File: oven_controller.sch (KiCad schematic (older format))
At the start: 31 parts, among them CON1 BUQ2-USB-MICRO-B, IC1 BUQ2-ATXMEGA128A4U-A, P1 CONN_THERMO, P2 CONN_POWER, U1 FLASH_MEMORY, U2 MAX6675ISA+, U3 TAG-CONNECT-ATMEL-PDI-CONNECT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, U4 LD1117-SOT-223, U5 LS013B4DN04, U6 SW_PUSH_4_PIN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

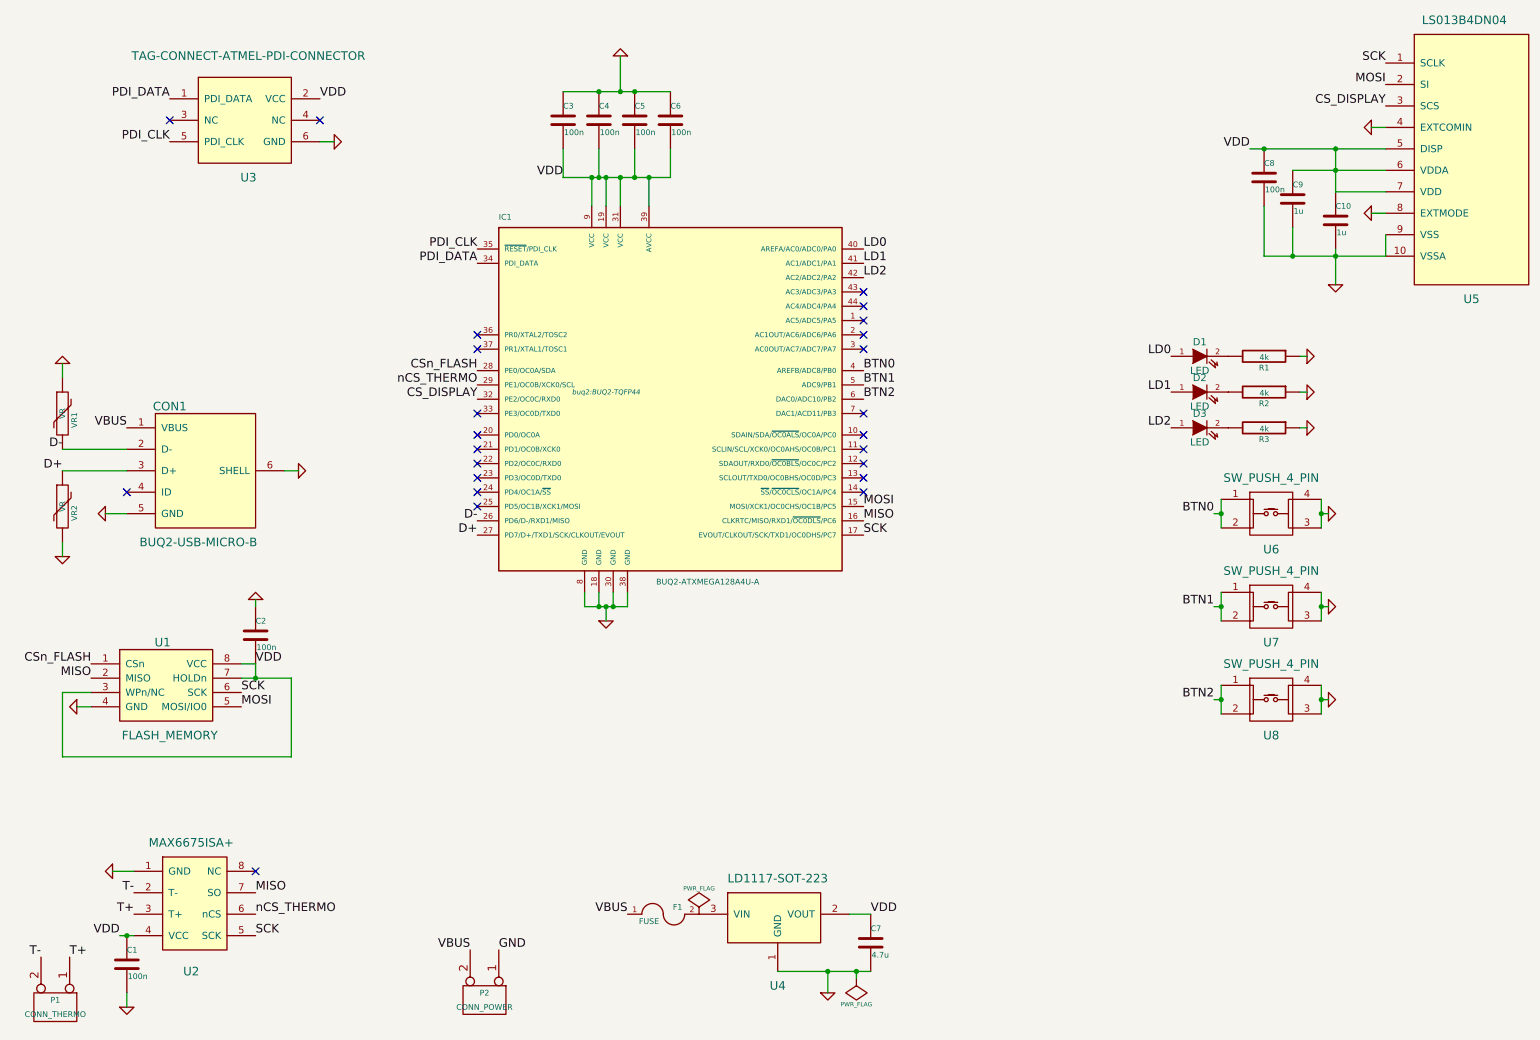
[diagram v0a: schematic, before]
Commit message: Layout done, but not checked
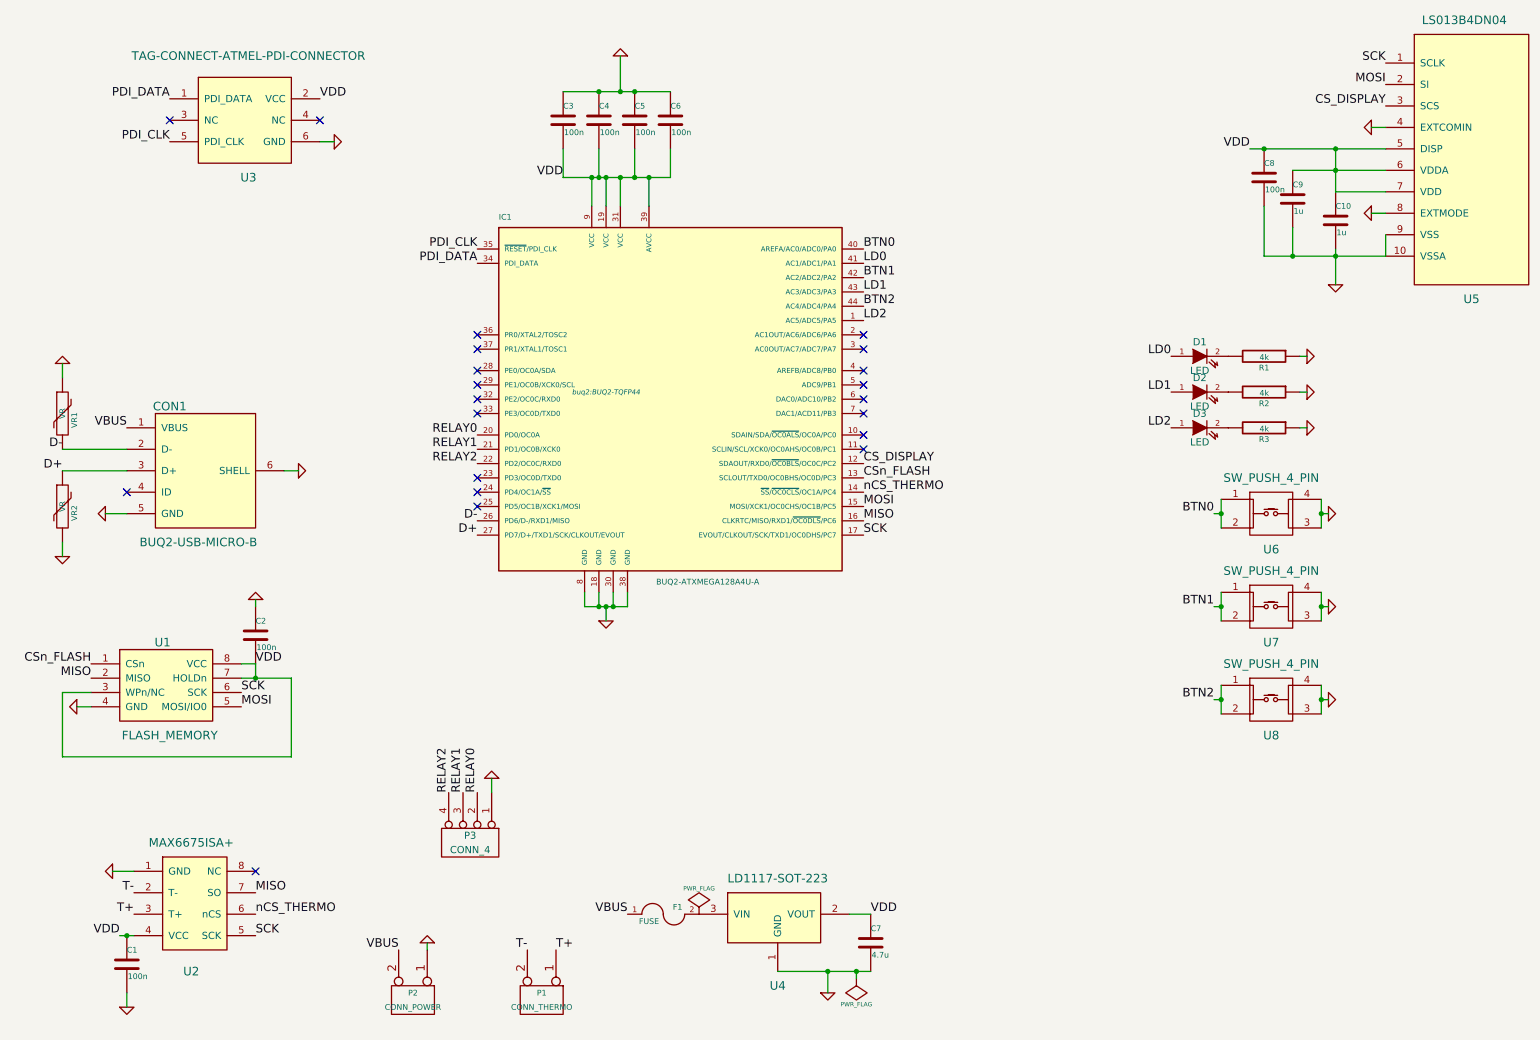
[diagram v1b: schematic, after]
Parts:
- added P3: CONN_4, buq2:PIN_HEADER_4, symbol CONN_4
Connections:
- net BTN0: now also IC1.40 (AREFA/AC0/ADC0/PA0); no longer IC1.4 (AREFB/ADC8/PB0)
- net BTN1: now also IC1.42 (AC2/ADC2/PA2); no longer IC1.5 (ADC9/PB1)
- net BTN2: now also IC1.44 (AC4/ADC4/PA4); no longer IC1.6 (DAC0/ADC10/PB2)
- net CS_DISPLAY: now also IC1.12 (SDAOUT/RXD0/~OC0BLS~/OC0C/PC2); no longer IC1.32 (PE2/OC0C/RXD0)
- net CSn_FLASH: now also IC1.13 (SCLOUT/TXD0/OC0BHS/OC0D/PC3); no longer IC1.28 (PE0/OC0A/SDA)
- net GND: now also P3.1 (P1)
- net LD0: now also IC1.41 (AC1/ADC1/PA1); no longer IC1.40 (AREFA/AC0/ADC0/PA0)
- net LD1: now also IC1.43 (AC3/ADC3/PA3); no longer IC1.41 (AC1/ADC1/PA1)
- net LD2: now also IC1.1 (AC5/ADC5/PA5); no longer IC1.42 (AC2/ADC2/PA2)
- net nCS_THERMO: now also IC1.14 (~SS~/~OC0CLS~/OC1A/PC4); no longer IC1.29 (PE1/OC0B/XCK0/SCL)
- net RELAY0: now reaches IC1.20 (PD0/OC0A)
- net RELAY0: now also P3.2 (P2)
- net RELAY1: now reaches IC1.21 (PD1/OC0B/XCK0)
- net RELAY1: now also P3.3 (P3)
- net RELAY2: now reaches IC1.22 (PD2/OC0C/RXD0)
- net RELAY2: now also P3.4 (P4)
- no-connect marks 24 -> 21
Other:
- moved on the sheet: P1, P2
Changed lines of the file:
@@
 Text Label 3650 4300 2    60   ~ 0
 D+
-Text Label 3650 3150 2    60   ~ 0
+Text Label 6350 3900 0    60   ~ 0
 CSn_FLASH
 Text Label 6350 4100 0    60   ~ 0
@@
 Text Label 2100 6950 0    60   ~ 0
 nCS_THERMO
-Text Label 3650 3250 2    60   ~ 0
+Text Label 6350 4000 0    60   ~ 0
 nCS_THERMO
 Text Label 2100 6800 0    60   ~ 0
@@
 L CONN_2 P1
 U 1 1 54BEA1D6
-P 700 7600
-F 0 "P1" V 650 7600 40  0000 C CNN
-F 1 "CONN_THERMO" V 750 7600 40  0000 C CNN
-F 2 "buq2:PIN_HEADER_2" H 700 7600 60  0001 C CNN
-F 3 "" H 700 7600 60  0000 C CNN
-	1    700  7600
-	0    1    1    0
-$EndComp
-Text Label 600  7250 2    60   ~ 0
+P 4100 7550
+F 0 "P1" V 4050 7550 40  0000 C CNN
+F 1 "CONN_THERMO" V 4150 7550 40  0000 C CNN
+F 2 "buq2:PIN_HEADER_2" H 4100 7550 60  0001 C CNN
+F 3 "" H 4100 7550 60  0000 C CNN
+	1    4100 7550
+	0    1    1    0
+$EndComp
+Text Label 4000 7200 2    60   ~ 0
 T-
-Text Label 800  7250 0    60   ~ 0
+Text Label 4200 7200 0    60   ~ 0
 T+
 $Comp
@@
 Text Label 10000 1150 2    60   ~ 0
 MOSI
-Text Label 3650 3350 2    60   ~ 0
+Text Label 6350 3800 0    60   ~ 0
 CS_DISPLAY
 Text Label 10000 1300 2    60   ~ 0
@@
 L CONN_2 P2
 U 1 1 54BEB6B2
-P 3700 7550
-F 0 "P2" V 3650 7550 40  0000 C CNN
-F 1 "CONN_POWER" V 3750 7550 40  0000 C CNN
-F 2 "buq2:PIN_HEADER_2" H 3700 7550 60  0001 C CNN
-F 3 "" H 3700 7550 60  0000 C CNN
-	1    3700 7550
-	0    1    1    0
-$EndComp
-Text Label 3600 7200 2    60   ~ 0
+P 3200 7550
+F 0 "P2" V 3150 7550 40  0000 C CNN
+F 1 "CONN_POWER" V 3250 7550 40  0000 C CNN
+F 2 "buq2:PIN_HEADER_2" H 3200 7550 60  0001 C CNN
+F 3 "" H 3200 7550 60  0000 C CNN
+	1    3200 7550
+	0    1    1    0
+$EndComp
+Text Label 3100 7200 2    60   ~ 0
 VBUS
-Text Label 3800 7200 0    60   ~ 0
-GND
 $Comp
 L LD1117-SOT-223 U4
@@
 Text Label 8800 4800 2    60   ~ 0
 BTN1
-Text Label 6350 3250 0    60   ~ 0
+Text Label 6350 2500 0    60   ~ 0
 BTN1
-Text Label 6350 3350 0    60   ~ 0
+Text Label 6350 2700 0    60   ~ 0
 BTN2
-Text Label 6350 3150 0    60   ~ 0
+Text Label 6350 2300 0    60   ~ 0
 BTN0
 $Comp
@@
 Text Label 8500 3550 2    60   ~ 0
 LD2
-Text Label 6350 2300 0    60   ~ 0
+Text Label 6350 2400 0    60   ~ 0
 LD0
-Text Label 6350 2400 0    60   ~ 0
+Text Label 6350 2600 0    60   ~ 0
 LD1
-Text Label 6350 2500 0    60   ~ 0
+Text Label 6350 2800 0    60   ~ 0
 LD2
 $Comp
@@
 	6300 7400 6300 7350
 Connection ~ 6300 7350
-NoConn ~ 6350 4000
-NoConn ~ 6350 3900
-NoConn ~ 6350 3800
+NoConn ~ 6350 3250
+NoConn ~ 6350 3350
+NoConn ~ 6350 3150
 NoConn ~ 6350 3700
 NoConn ~ 6350 3600
@@
 NoConn ~ 6350 3000
 NoConn ~ 6350 2900
-NoConn ~ 6350 2800
-NoConn ~ 6350 2700
-NoConn ~ 6350 2600
+NoConn ~ 3650 3150
+NoConn ~ 3650 3250
+NoConn ~ 3650 3350
 NoConn ~ 3650 2900
 NoConn ~ 3650 3000
 NoConn ~ 3650 3450
-NoConn ~ 3650 3600
-NoConn ~ 3650 3700
-NoConn ~ 3650 3800
 NoConn ~ 3650 3900
 NoConn ~ 3650 4000
@@
 	8850 4800 8800 4800
 Connection ~ 8850 4800
+$Comp
+L GND #PWR024
+U 1 1 54BF66A7
+P 3300 7150
+F 0 "#PWR024" H 3300 7150 30  0001 C CNN
+F 1 "GND" H 3300 7080 30  0001 C CNN
+F 2 "" H 3300 7150 60  0000 C CNN
+F 3 "" H 3300 7150 60  0000 C CNN
+	1    3300 7150
+	-1   0    0    1
+$EndComp
+Wire Wire Line
+	3300 7150 3300 7200
+$Comp
+L GND #PWR025
+U 1 1 54BF685A
+P 3750 6000
+F 0 "#PWR025" H 3750 6000 30  0001 C CNN
+F 1 "GND" H 3750 5930 30  0001 C CNN
+F 2 "" H 3750 6000 60  0000 C CNN
+F 3 "" H 3750 6000 60  0000 C CNN
+	1    3750 6000
+	-1   0    0    1
+$EndComp
+Text Label 3650 6100 1    60   ~ 0
+RELAY0
+Text Label 3650 3600 2    60   ~ 0
+RELAY0
+$Comp
+L CONN_4 P3
+U 1 1 54BFB3CC
+P 3600 6450
+F 0 "P3" V 3550 6450 50  0000 C CNN
+F 1 "CONN_4" V 3650 6450 50  0000 C CNN
+F 2 "buq2:PIN_HEADER_4" H 3600 6450 60  0001 C CNN
+F 3 "" H 3600 6450 60  0000 C CNN
+	1    3600 6450
+	0    1    1    0
+$EndComp
+Wire Wire Line
+	3750 6000 3750 6100
+Text Label 3550 6100 1    60   ~ 0
+RELAY1
+Text Label 3450 6100 1    60   ~ 0
+RELAY2
+Text Label 3650 3700 2    60   ~ 0
+RELAY1
+Text Label 3650 3800 2    60   ~ 0
+RELAY2
 $EndSCHEMATC

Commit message: Ordered v1
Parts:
- added C11: 100n, buq2:SM0603, symbol C
- added P4: CONN_THERMO1, buq2:PIN_HEADER_2, symbol CONN_2
- added U9: MAX6675ISA+, buq2:8-SOIC, symbol MAX6675ISA+
- P1: value CONN_THERMO -> CONN_THERMO0
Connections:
- net CS_DISPLAY: now also IC1.10 (SDAIN/SDA/~OC0ALS~/OC0A/PC0); no longer IC1.12 (SDAOUT/RXD0/~OC0BLS~/OC0C/PC2)
- net CSn_FLASH: now also IC1.11 (SCLIN/SCL/XCK0/OC0AHS/OC0B/PC1); no longer IC1.13 (SCLOUT/TXD0/OC0BHS/OC0D/PC3)
- net GND: now also C11.2, U9.1 (GND)
- net MISO: now also U9.7 (SO)
- net SCK: now also U9.5 (SCK)
- net VDD: now also C11.1, U9.4 (VCC)
- net T+ renamed T+0
- net T- renamed T-0
- net nCS_THERMO: no longer names the net of IC1.14 (~SS~/~OC0CLS~/OC1A/PC4)
- net nCS_THERMO: no longer U2.6 (nCS)
- new net T+1: P4.1 (P1), U9.3 (T+)
- new net T-1: P4.2 (PM), U9.2 (T-)
- new net nCS_THERMO0: IC1.13 (SCLOUT/TXD0/OC0BHS/OC0D/PC3), U2.6 (nCS)
- new net nCS_THERMO1: IC1.12 (SDAOUT/RXD0/~OC0BLS~/OC0C/PC2), U9.6 (nCS)
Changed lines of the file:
@@
 LIBS:valves
 LIBS:buq2-kicad-components
+LIBS:oven_controller-cache
 EELAYER 25 0
 EELAYER END
@@
 Text Label 3650 4300 2    60   ~ 0
 D+
-Text Label 6350 3900 0    60   ~ 0
+Text Label 6350 3700 0    60   ~ 0
 CSn_FLASH
 Text Label 6350 4100 0    60   ~ 0
@@
 VDD
 Text Label 1250 6950 2    60   ~ 0
-T+
+T+0
 Text Label 1250 6800 2    60   ~ 0
-T-
+T-0
 $Comp
 L GND #PWR04
@@
 	1100 6650 1250 6650
 Text Label 2100 6950 0    60   ~ 0
-nCS_THERMO
-Text Label 6350 4000 0    60   ~ 0
-nCS_THERMO
+nCS_THERMO0
+Text Label 6350 3900 0    60   ~ 0
+nCS_THERMO0
 Text Label 2100 6800 0    60   ~ 0
 MISO
@@
 P 4100 7550
 F 0 "P1" V 4050 7550 40  0000 C CNN
-F 1 "CONN_THERMO" V 4150 7550 40  0000 C CNN
+F 1 "CONN_THERMO0" V 4150 7550 40  0000 C CNN
 F 2 "buq2:PIN_HEADER_2" H 4100 7550 60  0001 C CNN
 F 3 "" H 4100 7550 60  0000 C CNN
@@
 $EndComp
 Text Label 4000 7200 2    60   ~ 0
-T-
+T-0
 Text Label 4200 7200 0    60   ~ 0
-T+
+T+0
 $Comp
 L LS013B4DN04 U5
@@
 Text Label 10000 1150 2    60   ~ 0
 MOSI
-Text Label 6350 3800 0    60   ~ 0
+Text Label 6350 3600 0    60   ~ 0
 CS_DISPLAY
 Text Label 10000 1300 2    60   ~ 0
@@
 NoConn ~ 6350 3350
 NoConn ~ 6350 3150
-NoConn ~ 6350 3700
-NoConn ~ 6350 3600
 NoConn ~ 6350 3450
 NoConn ~ 6350 3000
@@
 Text Label 3650 3800 2    60   ~ 0
 RELAY2
+$Comp
+L MAX6675ISA+ U9
+U 1 1 54BF378E
+P 5250 5600
+F 0 "U9" H 5250 5100 60  0000 C CNN
+F 1 "MAX6675ISA+" H 5250 6000 60  0000 C CNN
+F 2 "buq2:8-SOIC" H 5300 5350 60  0001 C CNN
+F 3 "" H 5300 5350 60  0000 C CNN
+	1    5250 5600
+	1    0    0    -1
+$EndComp
+$Comp
+L C C11
+U 1 1 54BF384C
+P 4600 6050
+F 0 "C11" H 4600 6150 40  0000 L CNN
+F 1 "100n" H 4606 5965 40  0000 L CNN
+F 2 "buq2:SM0603" H 4638 5900 30  0001 C CNN
+F 3 "" H 4600 6050 60  0000 C CNN
+	1    4600 6050
+	1    0    0    -1
+$EndComp
+$Comp
+L GND #PWR026
+U 1 1 54BF38B3
+P 4600 6350
+F 0 "#PWR026" H 4600 6350 30  0001 C CNN
+F 1 "GND" H 4600 6280 30  0001 C CNN
+F 2 "" H 4600 6350 60  0000 C CNN
+F 3 "" H 4600 6350 60  0000 C CNN
+	1    4600 6350
+	1    0    0    -1
+$EndComp
+Wire Wire Line
+	4600 6350 4600 6250
+Wire Wire Line
+	4600 5850 4850 5850
+Text Label 4850 5550 2    60   ~ 0
+T-1
+Text Label 4850 5700 2    60   ~ 0
+T+1
+Text Label 5700 5550 0    60   ~ 0
+MISO
+Text Label 5700 5700 0    60   ~ 0
+nCS_THERMO1
+Text Label 5700 5850 0    60   ~ 0
+SCK
+NoConn ~ 5700 5400
+$Comp
+L GND #PWR027
+U 1 1 54BF3CB5
+P 4700 5400
+F 0 "#PWR027" H 4700 5400 30  0001 C CNN
+F 1 "GND" H 4700 5330 30  0001 C CNN
+F 2 "" H 4700 5400 60  0000 C CNN
+F 3 "" H 4700 5400 60  0000 C CNN
+	1    4700 5400
+	0    1    1    0
+$EndComp
+Wire Wire Line
+	4700 5400 4850 5400
+Text Label 6350 3800 0    60   ~ 0
+nCS_THERMO1
+NoConn ~ 6350 4000
+$Comp
+L CONN_2 P4
+U 1 1 54BF48F3
+P 4800 7650
+F 0 "P4" V 4750 7650 40  0000 C CNN
+F 1 "CONN_THERMO1" V 4850 7650 40  0000 C CNN
+F 2 "buq2:PIN_HEADER_2" H 4800 7650 60  0001 C CNN
+F 3 "" H 4800 7650 60  0000 C CNN
+	1    4800 7650
+	0    1    1    0
+$EndComp
+Text Label 4700 7300 2    60   ~ 0
+T-1
+Text Label 4900 7300 0    60   ~ 0
+T+1
+Text Label 4600 5850 2    60   ~ 0
+VDD
 $EndSCHEMATC
